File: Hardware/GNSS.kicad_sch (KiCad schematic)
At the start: 27 parts, among them J1 U.FL, Q3 BSS138, U13 74HC4052D, U2 mosaic-X5

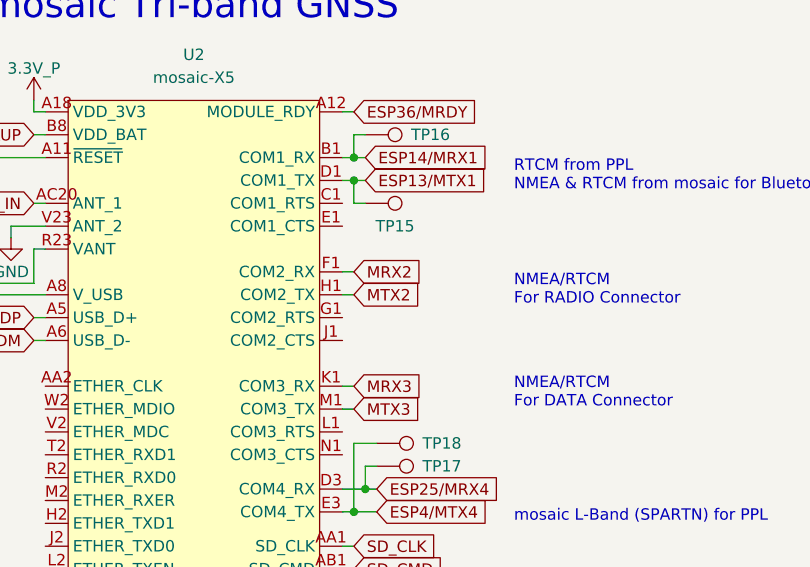
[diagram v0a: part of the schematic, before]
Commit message: Add SD_DET and 1A regulator
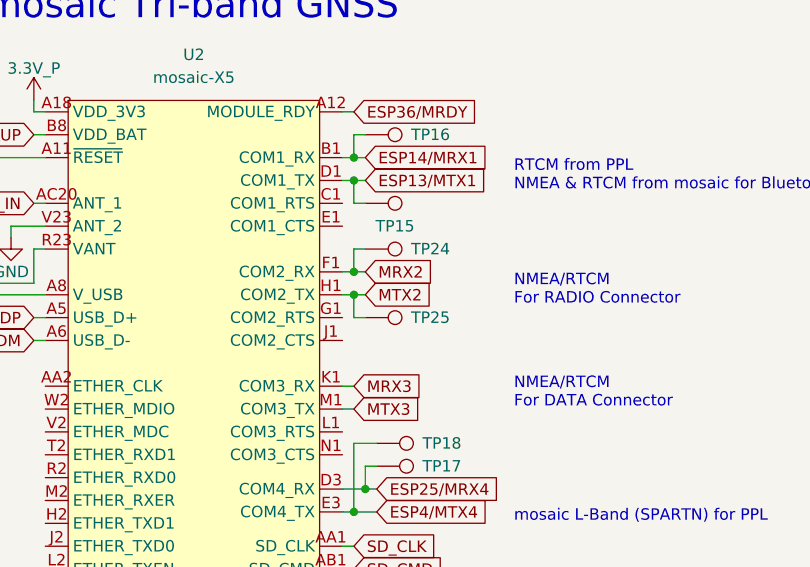
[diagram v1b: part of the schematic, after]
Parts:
- added TP24, TP25: 1.0mm, SparkFun-Connector:TestPoint-1.0mm, symbol SparkFun-Connector:TestPoint_1.0mm
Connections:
- net MRX2: now also TP24.1
- net MTX2: now also TP25.1
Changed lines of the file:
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@@
 	)
 	(junction
+		(at 99.06 48.26)
+		(diameter 0)
+		(color 0 0 0 0)
+	)
+	(junction
 		(at 231.14 137.16)
 		(diameter 0)
@@
 	)
 	(junction
+		(at 99.06 50.8)
+		(diameter 0)
+		(color 0 0 0 0)
+	)
+	(junction
 		(at 217.17 41.91)
 		(diameter 0)
@@
 	(wire
 		(pts
+			(xy 100.33 53.34) (xy 99.06 53.34)
+		)
+		(stroke
+			(width 0)
+			(type default)
+		)
+	)
+	(wire
+		(pts
 			(xy 92.71 182.88) (xy 91.44 182.88)
 		)
@@
 	(wire
 		(pts
-			(xy 99.06 50.8) (xy 97.79 50.8)
+			(xy 100.33 50.8) (xy 99.06 50.8)
 		)
 		(stroke
@@
 	(wire
 		(pts
+			(xy 99.06 50.8) (xy 97.79 50.8)
+		)
+		(stroke
+			(width 0)
+			(type default)
+		)
+	)
+	(wire
+		(pts
 			(xy 63.5 116.84) (xy 64.77 116.84)
 		)
@@
 	(wire
 		(pts
+			(xy 99.06 50.8) (xy 99.06 53.34)
+		)
+		(stroke
+			(width 0)
+			(type default)
+		)
+	)
+	(wire
+		(pts
 			(xy 53.34 114.3) (xy 54.61 114.3)
 		)
@@
 	(wire
 		(pts
-			(xy 99.06 48.26) (xy 97.79 48.26)
+			(xy 100.33 48.26) (xy 99.06 48.26)
 		)
 		(stroke
@@
 	(wire
 		(pts
+			(xy 99.06 48.26) (xy 97.79 48.26)
+		)
+		(stroke
+			(width 0)
+			(type default)
+		)
+	)
+	(wire
+		(pts
 			(xy 231.14 135.89) (xy 231.14 137.16)
 		)
@@
 	(wire
 		(pts
+			(xy 99.06 45.72) (xy 99.06 48.26)
+		)
+		(stroke
+			(width 0)
+			(type default)
+		)
+	)
+	(wire
+		(pts
 			(xy 92.71 180.34) (xy 91.44 180.34)
 		)
@@
 	(wire
 		(pts
+			(xy 100.33 45.72) (xy 99.06 45.72)
+		)
+		(stroke
+			(width 0)
+			(type default)
+		)
+	)
+	(wire
+		(pts
 			(xy 223.52 135.89) (xy 223.52 137.16)
 		)
@@
 	(global_label "MTX2"
 		(shape input)
-		(at 99.06 50.8 0)
+		(at 100.33 50.8 0)
 		(fields_autoplaced yes)
 		(effects
@@
 		)
 		(property "Intersheetrefs" "${INTERSHEET_REFS}"
-			(at 106.8832 50.8 0)
+			(at 108.1532 50.8 0)
 			(effects
 				(font
@@
 	(global_label "MRX2"
 		(shape input)
-		(at 99.06 48.26 0)
+		(at 100.33 48.26 0)
 		(fields_autoplaced yes)
 		(effects
@@
 		)
 		(property "Intersheetrefs" "${INTERSHEET_REFS}"
-			(at 107.1856 48.26 0)
+			(at 108.4556 48.26 0)
 			(effects
 				(font
@@
 	)
 	(symbol
+		(lib_id "SparkFun-Connector:TestPoint_1.0mm")
+		(at 100.33 53.34 270)
+		(unit 1)
+		(exclude_from_sim no)
+		(in_bom yes)
+		(on_board yes)
+		(dnp no)
+		(fields_autoplaced yes)
+		(property "Reference" "TP25"
+			(at 105.41 53.3399 90)
+			(effects
+				(font
+					(size 1.27 1.27)
+				)
+				(justify left)
+			)
+		)
+		(property "Value" "1.0mm"
+			(at 96.52 53.34 0)
+			(effects
+				(font
+					(size 1.27 1.27)
+				)
+				(hide yes)
+			)
+		)
+		(property "Footprint" "SparkFun-Connector:TestPoint-1.0mm"
+			(at 93.98 53.34 0)
+			(effects
+				(font
+					(size 1.27 1.27)
+				)
+				(hide yes)
+			)
+		)
+		(property "Datasheet" "~"
+			(at 92.71 53.34 0)
+			(effects
+				(font
+					(size 1.27 1.27)
+				)
+				(hide yes)
+			)
+		)
+		(property "Description" "Test Point"
+			(at 100.33 53.34 0)
+			(effects
+				(font
+					(size 1.27 1.27)
+				)
+				(hide yes)
+			)
+		)
+		(pin "1"
+		)
+		(instances
+			(project "SparkFun_RTK_Facet_mosaic"
+				(path "/e3dd3ae4-244d-4cba-9cca-5d2abf83f29a/1004b21d-c362-4c5d-adad-4952c3ff3811"
+					(reference "TP25")
+					(unit 1)
+				)
+			)
+		)
+	)
+	(symbol
 		(lib_id "SparkFun-Capacitor:0.1uF_0402_6.3V_10%")
 		(at 36.83 35.56 270)
@@
 					(unit 1)
 				)
+			)
+		)
+	)
+	(symbol
+		(lib_id "SparkFun-Connector:TestPoint_1.0mm")
+		(at 100.33 45.72 270)
+		(unit 1)
+		(exclude_from_sim no)
+		(in_bom yes)
+		(on_board yes)
+		(dnp no)
+		(fields_autoplaced yes)
+		(property "Reference" "TP24"
+			(at 105.41 45.7199 90)
+			(effects
+				(font
+					(size 1.27 1.27)
+				)
+				(justify left)
+			)
+		)
+		(property "Value" "1.0mm"
+			(at 96.52 45.72 0)
+			(effects
+				(font
+					(size 1.27 1.27)
+				)
+				(hide yes)
+			)
+		)
+		(property "Footprint" "SparkFun-Connector:TestPoint-1.0mm"
+			(at 93.98 45.72 0)
+			(effects
+				(font
+					(size 1.27 1.27)
+				)
+				(hide yes)
+			)
+		)
+		(property "Datasheet" "~"
+			(at 92.71 45.72 0)
+			(effects
+				(font
+					(size 1.27 1.27)
+				)
+				(hide yes)
+			)
+		)
+		(property "Description" "Test Point"
+			(at 100.33 45.72 0)
+			(effects
+				(font
+					(size 1.27 1.27)
+				)
+				(hide yes)
+			)
+		)
+		(pin "1"
+		)
+		(instances
+			(project "SparkFun_RTK_Facet_mosaic"
+				(path "/e3dd3ae4-244d-4cba-9cca-5d2abf83f29a/1004b21d-c362-4c5d-adad-4952c3ff3811"
+					(reference "TP24")
+					(unit 1)
+				)
